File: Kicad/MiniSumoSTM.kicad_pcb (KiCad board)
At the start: 2 copper layers, 93 x 88.1 mm, 63 parts, among them J10 Conn_01x03_Pin, J2 USB_B_Micro, J4 Conn_02x03_Top_Bottom, J5 Conn_02x03_Top_Bottom, J6 Conn_02x03_Top_Bottom, J7 Conn_02x03_Top_Bottom, J8 Conn_02x03_Top_Bottom, M1 Conn_01x02_Pin, M2 Conn_01x02_Pin, Q3 AON7422G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

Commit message: finished pcb
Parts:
- renumbered Battery_Pin1 to Batt_Pin
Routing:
- net GND: vias 317 -> 534
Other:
- outline, holes or cut-outs redrawn
- board text added: "{ "ViaStitching": "0.2", "stitch_zone_0": { "HSpacing": "1", "VSpacing": "1", "HOffset": "0", "VOffset": "0", "Clearance": "0.256", "Randomize": false } }"
- board text added: "{ "ViaStitching": "0.2", "stitch_zone_0": { "HSpacing": "1", "VSpacing": "1", "HOffset": "1", "VOffset": "1", "Clearance": "0.256", "Randomize": false } }"
- board text added: "{ "ViaStitching": "0.2", "stitch_zone_0": { "HSpacing": "1.5", "VSpacing": "1.5", "HOffset": "1.5", "VOffset": "1.5", "Clearance": "0.256", "Randomize": false } }"

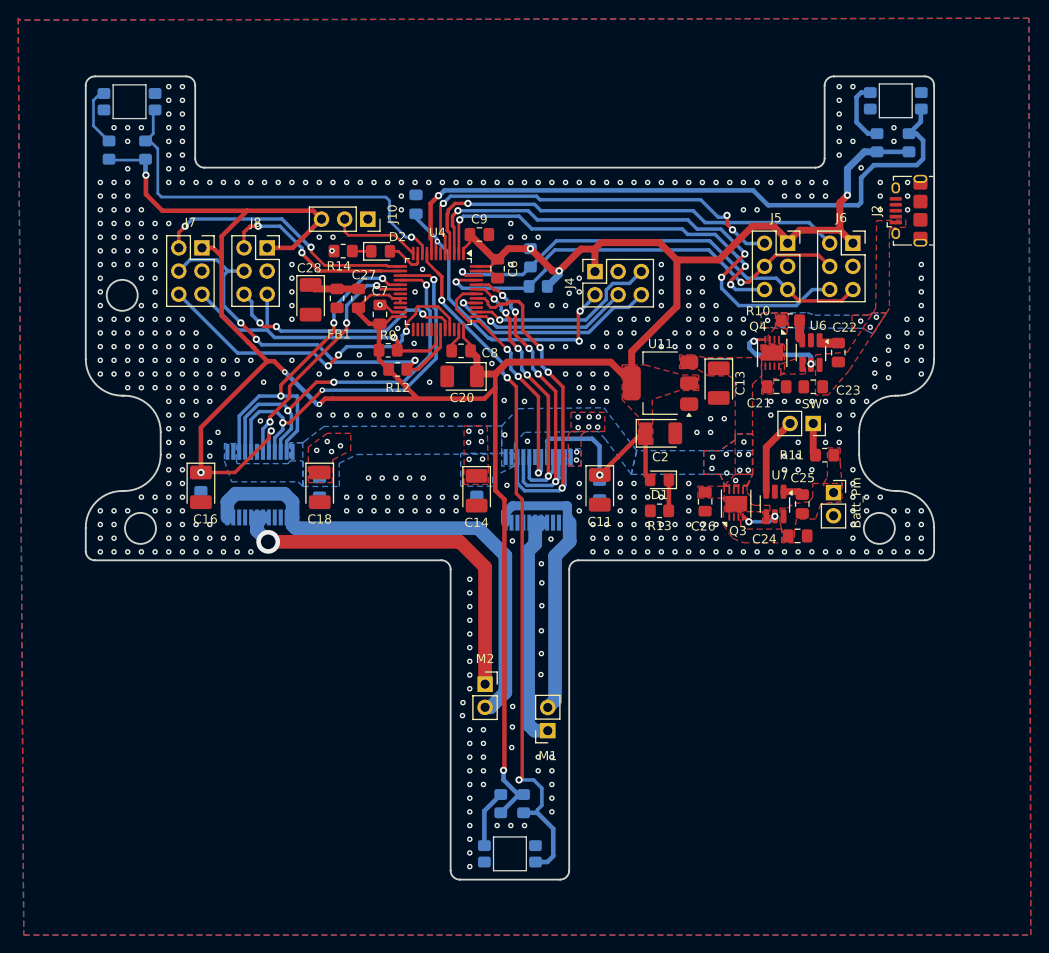
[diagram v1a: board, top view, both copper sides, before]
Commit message: finished pcb - added pwm resistors, and fixed VDDA decoupling
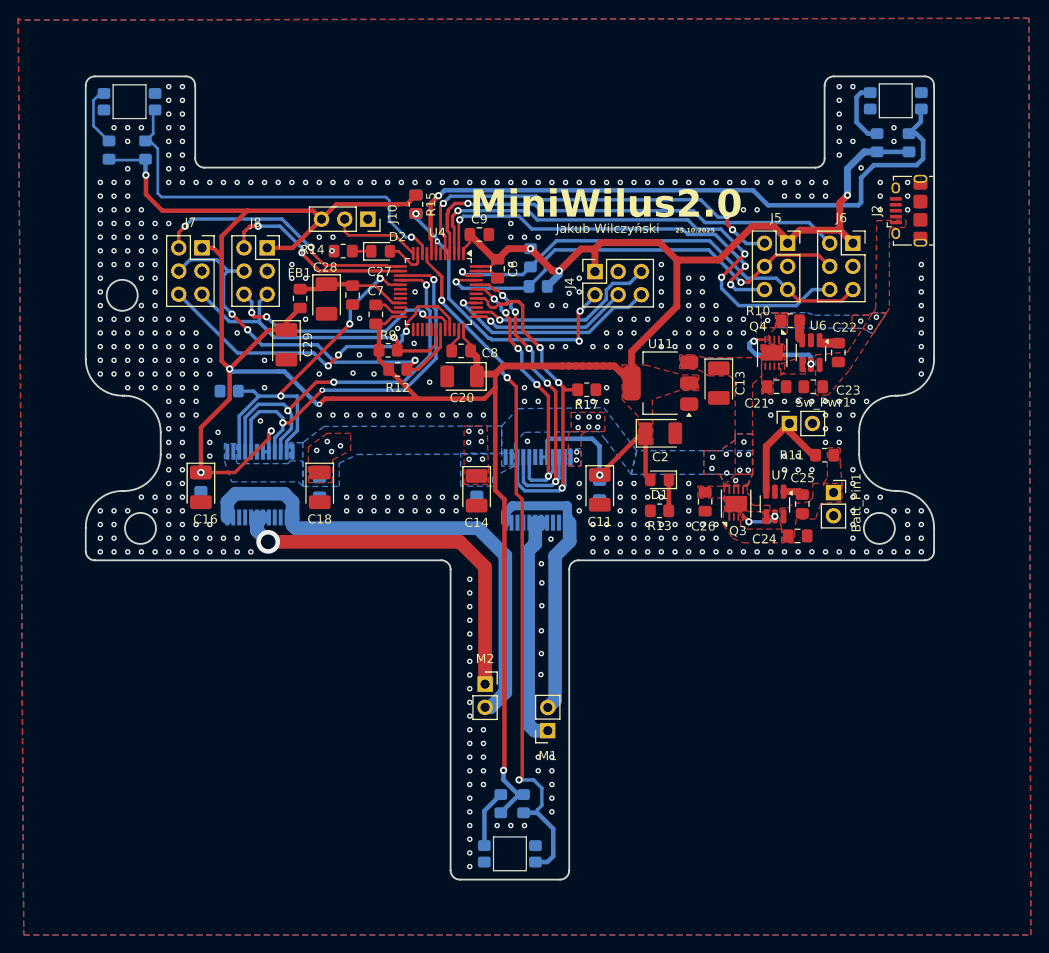
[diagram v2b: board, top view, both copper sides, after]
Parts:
- added C29: 10u, Capacitor_Tantalum_SMD:CP_EIA-3528-12_Kemet-T_HandSolder, F.Cu at (126.5, 83.9)
- added R15: 1k5, Resistor_SMD:R_0805_2012Metric_Pad1.20x1.40mm_HandSolder, F.Cu at (140.7, 68.5)
- added R16: 1k5, Resistor_SMD:R_0805_2012Metric_Pad1.20x1.40mm_HandSolder, B.Cu at (120.2, 89.0)
- added R17: 1k5, Resistor_SMD:R_0805_2012Metric_Pad1.20x1.40mm_HandSolder, F.Cu at (159.4, 88.8)
- R11: value 10k -> 100k
- moved FB1 6.40 mm to (128.0, 78.8), turned to -90 degrees
- moved Sw_Pwr1 2.62 mm to (181.6, 92.5), turned to 90 degrees
- moved C28 1.75 mm to (130.9, 78.9)
- moved C27 1.74 mm to (133.8, 78.5)
- moved C7 0.45 mm to (136.3, 80.6)
- renumbered Batt_Pin to Batt_Pin1, SW to Sw_Pwr1
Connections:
- C27 pad 1: /MCU/FERRITE -> +3.3VA
- C28 pad 1: /MCU/FERRITE -> +3.3VA
- FB1 pad 1: +3.3V -> +3.3VA
- FB1 pad 2: /MCU/FERRITE -> +3.3V
- R11 pad 1: Net-(Switch_Power1-Pin_1) -> /voltage_supply/ideal_diode_batt/EN
- Sw_Pwr1 pad 1: Net-(Switch_Power1-Pin_1) -> /voltage_supply/ideal_diode_batt/EN
- Sw_Pwr1 pad 2: /voltage_supply/ideal_diode_batt/EN -> GND
- U4 pad 18: /MCU/STBY1 -> unconnected-(U4-PB2-Pad18)
- U4 pad 20: +3.3V -> /MCU/VDDA
- U4 pad 21: +3.3V -> +3.3VA
- U4 pad 42: /MCU/STBY2 -> unconnected-(U4-PB5-Pad42)
- U8 pad 19: /MCU/STBY2 -> +3.3V
- U9 pad 19: /MCU/STBY1 -> +3.3V
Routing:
- net /MCU/STBY2: track 27.8 -> 0.00 mm, vias 3 -> 0
- net /MCU/STBY1: track 26.8 -> 0.00 mm, vias 3 -> 0
- net +3.3V: track 325.9 -> 341.0 mm
- net +3.3VA: track 0.00 -> 12.1 mm
- net /MCU/FERRITE: track 5.50 -> 0.00 mm
- net /voltage_supply/ideal_diode_batt/EN: track 8.56 -> 13.7 mm
- net Net-(Switch_Power1-Pin_1): track 3.58 -> 0.00 mm
- net /MCU/PWM2: track 39.8 -> 41.5 mm
- net /MCU/PWM1: track 38.8 -> 40.2 mm
- net /MCU/SDA2: track 34.7 -> 35.4 mm
- net GND: vias 534 -> 491
- net /MCU/NRESET: vias 3 -> 4
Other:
- board text added: "25.10.2025"
- board text added: "Jakub Wilczyński"
- board text added: "MiniWilus2.0"
- board text added: "{ "ViaStitching": "0.2", "stitch_zone_0": { "HSpacing": "2", "VSpacing": "2", "HOffset": "2", "VOffset": "2", "Clearance": "0.256", "Randomize": false } }"

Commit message: not small changes
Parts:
- removed J5, J6, J7, J8: Conn_02x03_Top_Bottom, Connector_PinSocket_2.54mm:PinSocket_2x03_P2.54mm_Vertical
- added TF1: Conn_02x03_Top_Bottom, Connector_PinHeader_2.54mm:PinHeader_2x03_P2.54mm_Vertical, F.Cu at (178.9, 72.8)
- added TF2: Conn_02x03_Top_Bottom, Connector_PinHeader_2.54mm:PinHeader_2x03_P2.54mm_Vertical, F.Cu at (186.2, 72.7)
- added TF3: Conn_02x03_Top_Bottom, Connector_PinHeader_2.54mm:PinHeader_2x03_P2.54mm_Vertical, F.Cu at (114.7, 73.3)
- added TF4: Conn_02x03_Top_Bottom, Connector_PinHeader_2.54mm:PinHeader_2x03_P2.54mm_Vertical, F.Cu at (121.8, 73.3)
- Batt_Pin1, Sw_Pwr1: footprint Connector_PinSocket_2.54mm:PinSocket_1x02_P2.54mm_Vertical -> Connector_PinHeader_2.54mm:PinHeader_1x02_P2.54mm_Vertical
- J10: footprint Connector_PinSocket_2.54mm:PinSocket_1x03_P2.54mm_Vertical -> Connector_PinHeader_2.54mm:PinHeader_1x03_P2.54mm_Vertical
- J4: footprint Connector_PinSocket_2.54mm:PinSocket_2x03_P2.54mm_Vertical -> Connector_PinHeader_2.54mm:PinHeader_2x03_P2.54mm_Vertical
- Q3, Q4: footprint Package_DFN_QFN:DFN-8-1EP_3x3mm_P0.5mm_EP1.7x2.4mm -> Package_DFN_QFN:DFN-8-1EP_3x3mm_P0.65mm_EP1.5x2.25mm
- moved J10 28.3 mm to (114.9, 89.6), turned to 180 degrees
- moved J4 2.59 mm to (160.3, 78.5)
- moved J2 2.38 mm to (194.7, 71.6)
- moved R1 2.26 mm to (194.4, 64.0)
- moved R2 2.26 mm to (190.9, 64.0)
- moved U1 2.26 mm to (192.9, 59.4)
- moved U2 2.22 mm to (109.9, 59.4)
- moved R3 1.25 mm to (107.1, 63.8)
- moved R4 1.25 mm to (111.1, 63.8)
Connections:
- J4 pad 1: +3.3V -> /MCU/NRESET
- J4 pad 2: /MCU/NRESET -> +3.3V
- J4 pad 3: GND -> /MCU/SWDIO
- J4 pad 4: /MCU/SWDIO -> GND
- J4 pad 5: /MCU/SWCLK -> /MCU/SWO
- J4 pad 6: /MCU/SWO -> /MCU/SWCLK
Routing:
- net /MCU/STARTER: track 9.88 -> 49.9 mm, vias 0 -> 1
- net /MCU/LS3: track 44.2 -> 38.2 mm
- net /MCU/LS1: track 71.3 -> 68.4 mm
- net +3.3V: track 341.0 -> 342.3 mm
- net /MCU/SWDIO: track 17.5 -> 18.2 mm
- net /MCU/PWM2: track 41.5 -> 40.8 mm
- net GND: vias 491 -> 452
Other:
- board size 93 x 88.1 mm -> 93 x 85.8 mm
- board text added: "+"
- board text added: "+3.3V"
- board text added: "-"
- board text added: "3.3V"
- board text added: "EX"
- board text added: "GND"
- board text added: "NR"
- board text added: "SCL"
- board text added: "SDA"
- board text added: "STARTER"
- board text added: "STRT"
- board text added: "SWCLK"
- board text added: "SWDIO"
- board text added: "SWO"
- board text added: "XS"
